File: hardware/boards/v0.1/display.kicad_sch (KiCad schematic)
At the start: 10 parts, among them U26 ER-TFT028A-4, U37 ER-TPC028-4.1

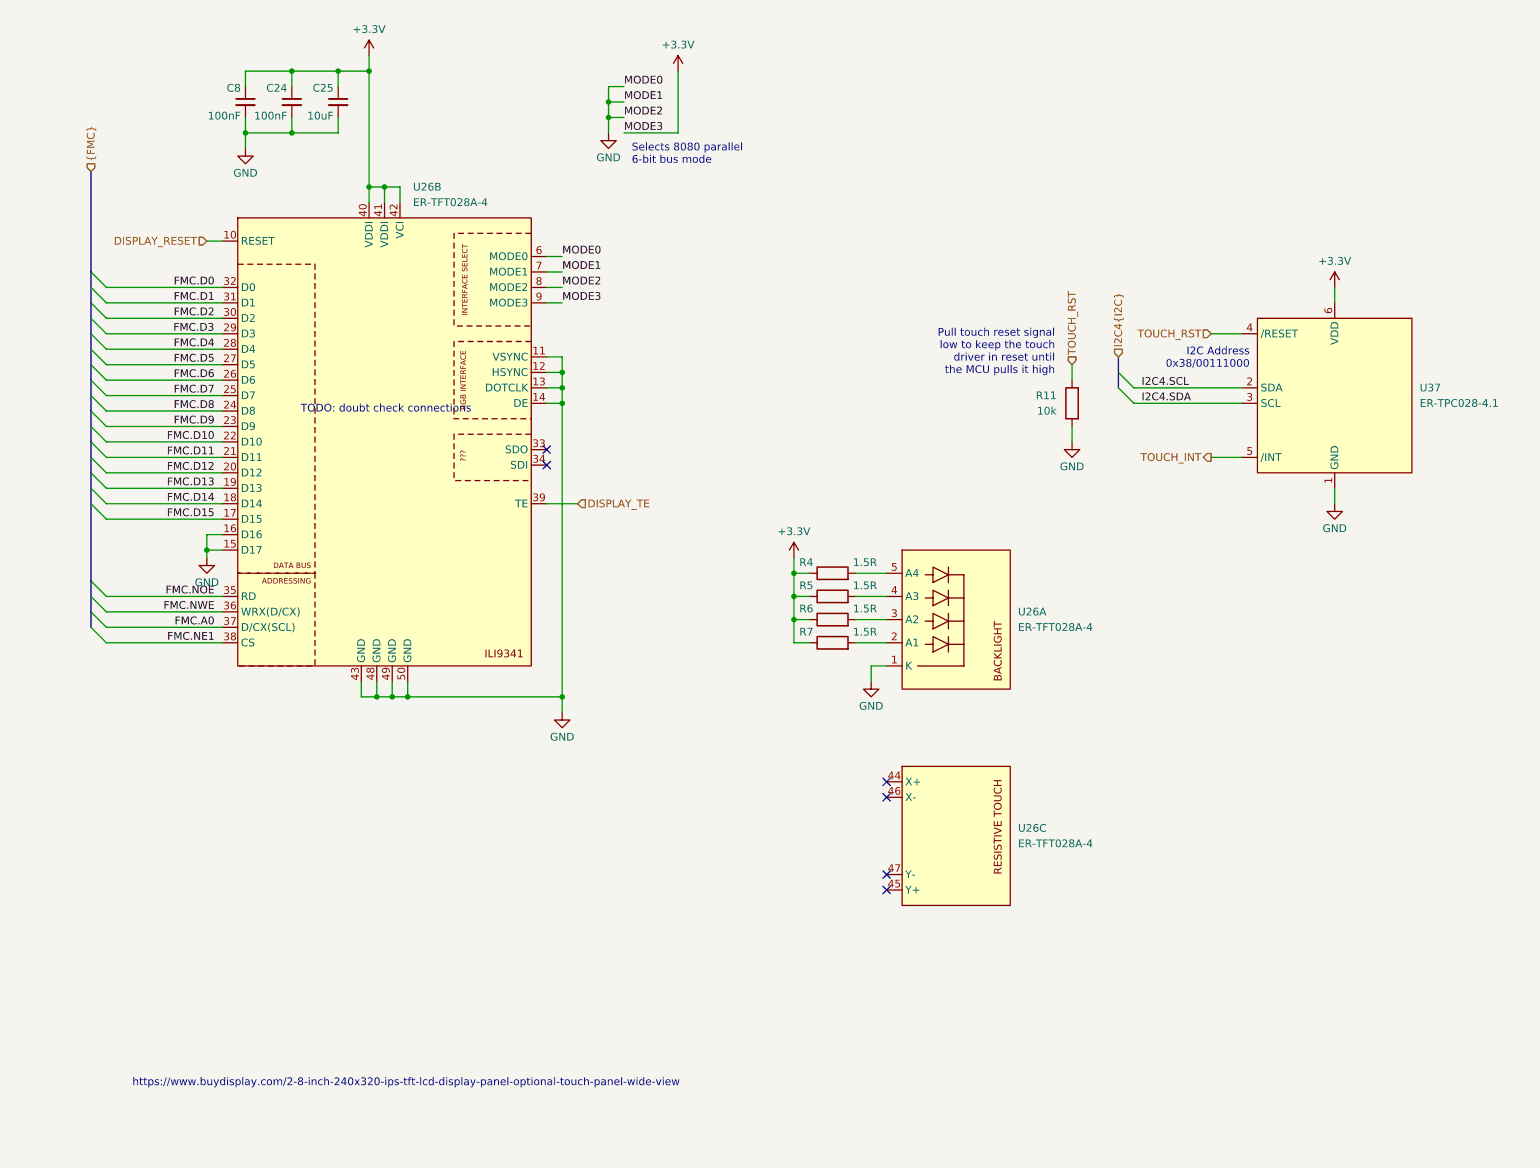
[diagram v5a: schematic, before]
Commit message: feat: add LCD backlight control
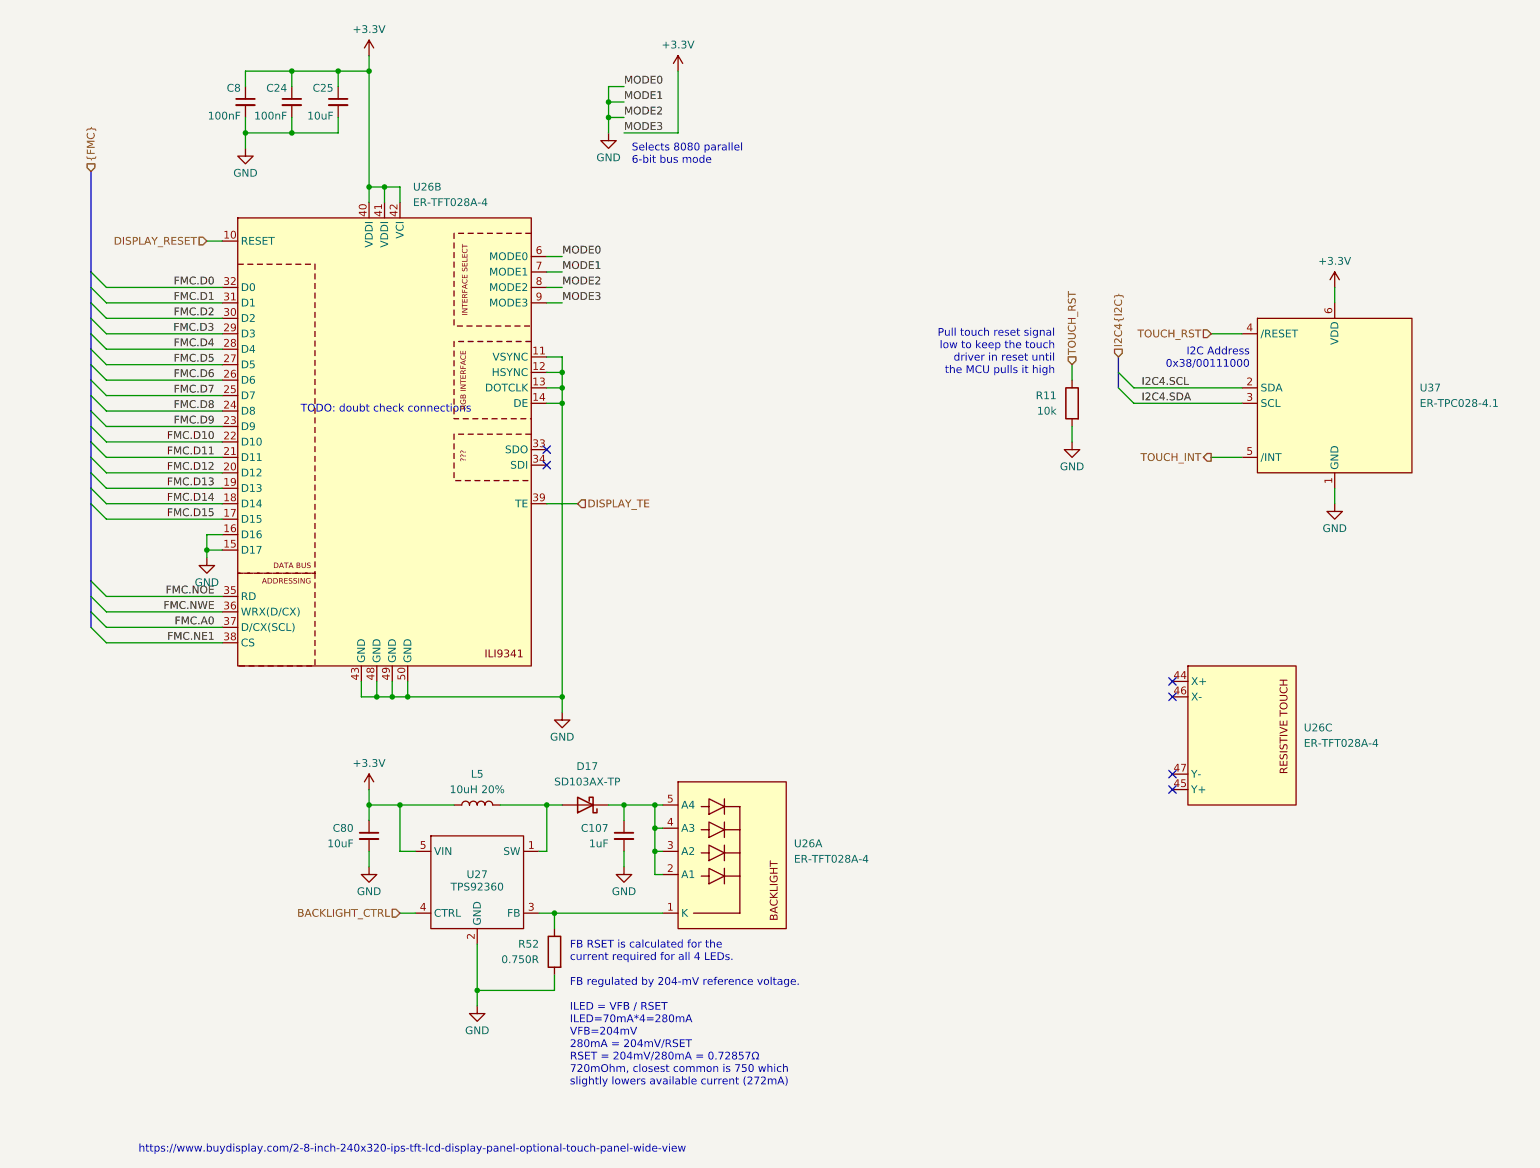
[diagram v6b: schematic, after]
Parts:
- removed R4, R5, R6, R7: 1.5R, Resistor_SMD:R_0402_1005Metric, symbol Device:R
- added C107: 1uF, Capacitor_SMD:C_0402_1005Metric, symbol Device:C_Small
- added C80: 10uF, Capacitor_SMD:C_0402_1005Metric, symbol Device:C_Small
- added D17: SD103AX-TP, Diode_SMD:D_SOD-523, symbol Device:D_Schottky
- added L5: 10uH 20%, Inductor_SMD:L_0805_2012Metric, symbol Device:L
- added R52: 0.750R, Resistor_SMD:R_0402_1005Metric, symbol Device:R
- added U27: TPS92360, Package_TO_SOT_SMD:SOT-353_SC-70-5, symbol pocket_synth:TPS92360DCKR
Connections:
- net +3.3V: now also C80.1, L5.1, U27.5 (VIN)
- net GND: now also C107.2, C80.2, R52.2, U27.2 (GND); no longer U26.1 (K)
- net at U26.4 (A3): now also U26.2 (A1), U26.3 (A2), U26.5 (A4), C107.1, D17.1 (K)
- new net: D17.2 (A), L5.2, U27.1 (SW)
- new net: R52.1, U26.1 (K), U27.3 (FB)
- new net BACKLIGHT_CTRL: U27.4 (CTRL)
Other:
- note added: "FB RSET is calculated for the current required for all 4 LEDs. FB regulated by 204-mV reference voltage. ILED = VFB / RSET ILED=70mA*4=280mA VFB=204mV 280mA = 204mV/RSET RSET = 204mV/280mA = 0.72857Ω 720mOhm, closest common is 750 which slightly lowers available current (272mA)"
- moved on the sheet: U26A, U26C

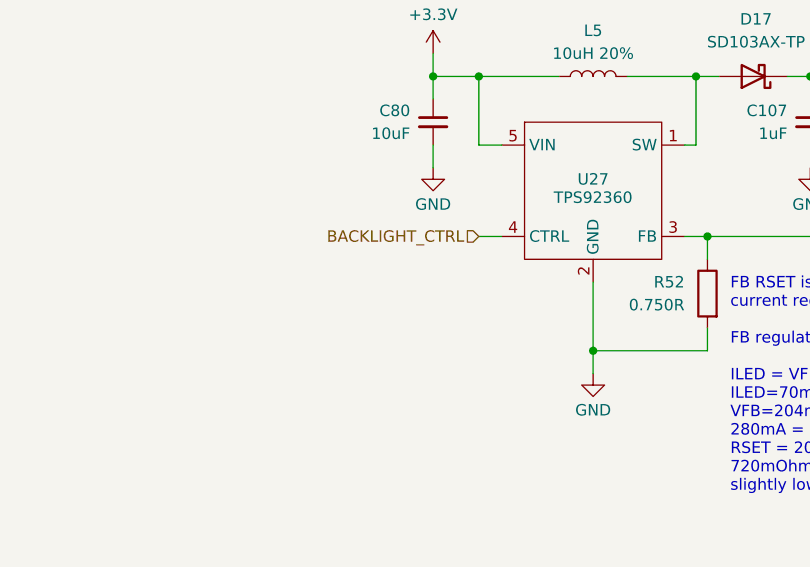
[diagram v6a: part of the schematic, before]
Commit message: feat: add power LEDs and adjust layout
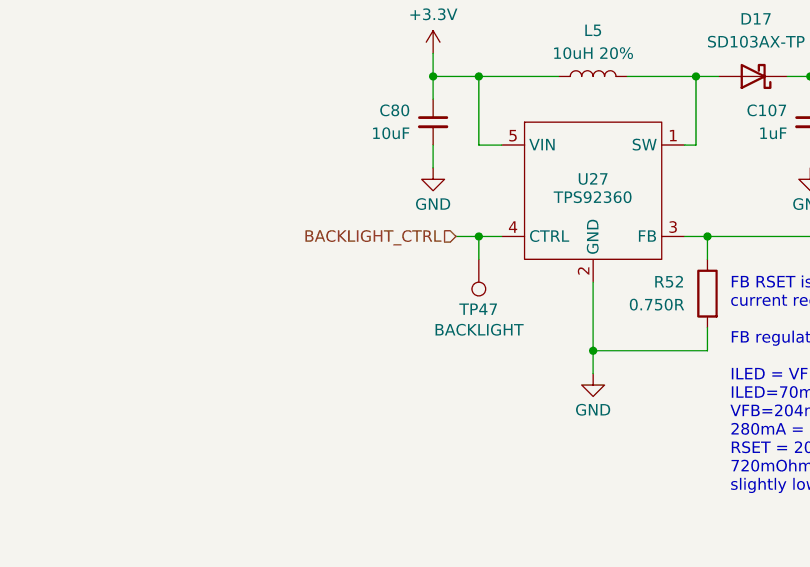
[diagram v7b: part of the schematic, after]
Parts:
- added TP47: BACKLIGHT, TestPoint:TestPoint_Pad_D1.0mm, symbol Connector:TestPoint
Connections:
- net BACKLIGHT_CTRL: now also TP47.1
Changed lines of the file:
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@@
 	)
 	(junction
+		(at 68.58 166.37)
+		(diameter 0)
+		(color 0 0 0 0)
+	)
+	(junction
 		(at 50.8 38.1)
 		(diameter 0)
@@
 	(wire
 		(pts
+			(xy 68.58 166.37) (xy 68.58 168.91)
+		)
+		(stroke
+			(width 0)
+			(type default)
+		)
+	)
+	(wire
+		(pts
 			(xy 36.83 55.88) (xy 39.37 55.88)
 		)
@@
 	(wire
 		(pts
-			(xy 68.58 166.37) (xy 71.12 166.37)
+			(xy 66.04 166.37) (xy 68.58 166.37)
 		)
 		(stroke
@@
 	(wire
 		(pts
+			(xy 68.58 166.37) (xy 71.12 166.37)
+		)
+		(stroke
+			(width 0)
+			(type default)
+		)
+	)
+	(wire
+		(pts
 			(xy 91.44 166.37) (xy 93.98 166.37)
 		)
@@
 	(hierarchical_label "BACKLIGHT_CTRL"
 		(shape input)
-		(at 68.58 166.37 180)
+		(at 66.04 166.37 180)
 		(effects
 			(font
@@
 					(unit 1)
 				)
+			)
+		)
+	)
+	(symbol
+		(lib_id "Connector:TestPoint")
+		(at 68.58 168.91 180)
+		(unit 1)
+		(exclude_from_sim no)
+		(in_bom no)
+		(on_board yes)
+		(dnp no)
+		(property "Reference" "TP47"
+			(at 68.58 174.498 0)
+			(effects
+				(font
+					(size 1.27 1.27)
+				)
+			)
+		)
+		(property "Value" "BACKLIGHT"
+			(at 68.58 176.784 0)
+			(effects
+				(font
+					(size 1.27 1.27)
+				)
+			)
+		)
+		(property "Footprint" "TestPoint:TestPoint_Pad_D1.0mm"
+			(at 63.5 168.91 0)
+			(effects
+				(font
+					(size 1.27 1.27)
+				)
+				(hide yes)
+			)
+		)
+		(property "Datasheet" "~"
+			(at 63.5 168.91 0)
+			(effects
+				(font
+					(size 1.27 1.27)
+				)
+				(hide yes)
+			)
+		)
+		(property "Description" "test point"
+			(at 68.58 168.91 0)
+			(effects
+				(font
+					(size 1.27 1.27)
+				)
+				(hide yes)
+			)
+		)
+		(pin "1"
+		)
+		(instances
+			(project "pocket_synth"
+				(path "/485383b8-00f4-4405-b270-de249939cff4/f0d5f3c5-7c53-4584-b479-82b3ef9bea09"
+					(reference "TP47")
+					(unit 1)
+				)

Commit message: feat: change charger, fuel gauge, and battery connector, re-route power system
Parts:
- C107: JLC C14445 -> C52923
- D17: JLC (none) -> C668989
- R11: JLC C25531 -> C25744
- U27: JLC (none) -> C2928788
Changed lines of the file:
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@@
+			)
+		)
+		(property "JLC" "C2928788"
+			(at 81.28 161.29 0)
+			(effects
+				(font
+					(size 1.27 1.27)
+				)
+				(hide yes)
 			)
 		)
@@
 			)
 		)
-		(property "JLC" "C25531"
+		(property "JLC" "C25744"
 			(at 179.07 82.55 0)
 			(effects
@@
 			)
 		)
-		(property "JLC" "C14445"
+		(property "JLC" "C52923"
 			(at 105.41 153.67 0)
 			(effects
@@
 			(at 99.06 148.59 0)
 			(effects
+				(font
+					(size 1.27 1.27)
+				)
+				(hide yes)
+			)
+		)
+		(property "JLC" "C668989"
+			(at 99.06 148.59 0)
+			(effects
